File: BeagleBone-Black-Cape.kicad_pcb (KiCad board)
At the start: 4 copper layers, 61.9 x 92.1 mm, 77 parts, among them J501 Conn_ARM_JTAG_SWD_10, J502 3.3V, P101 BeagleBone_Black_Header, P102 BeagleBone_Black_Header, U401 LM3671, U601 cc1352p, U602 MX25R8035FZUIL0, Y601 32.768kHz, Y602 48MHz

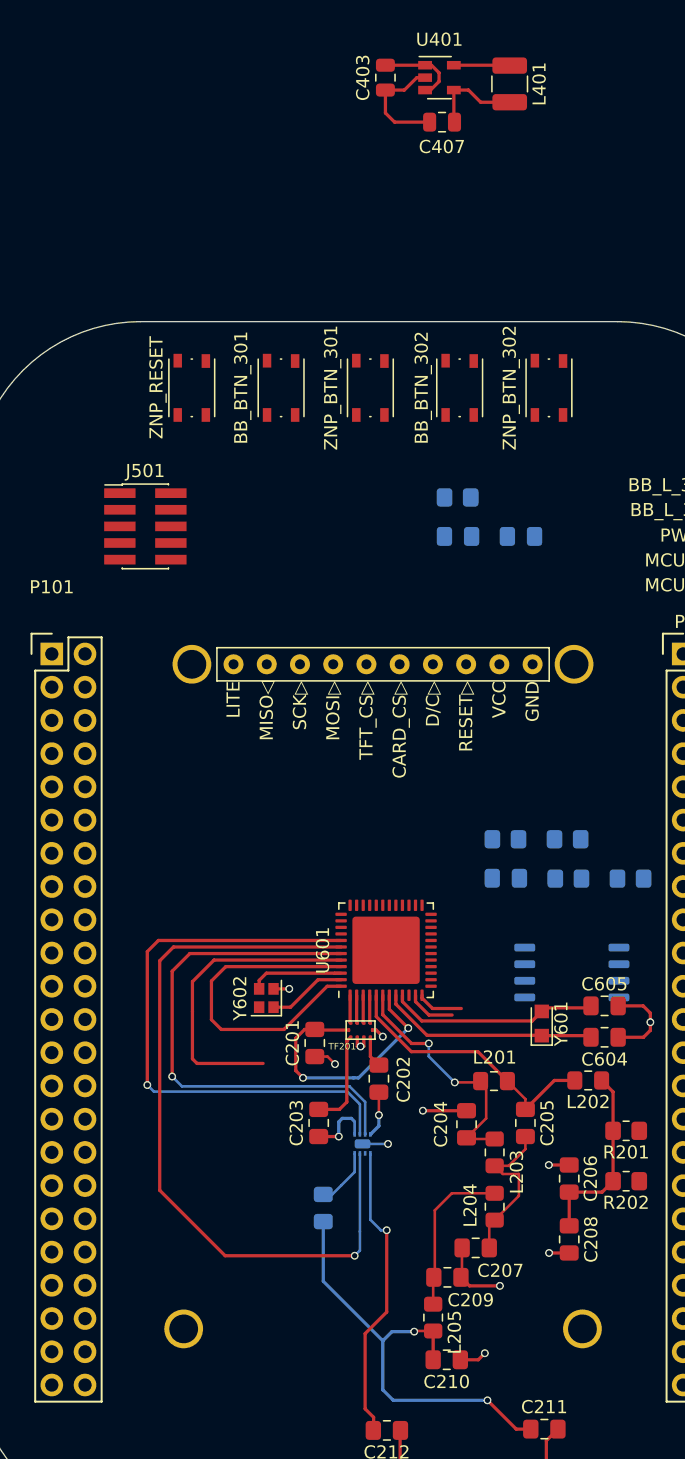
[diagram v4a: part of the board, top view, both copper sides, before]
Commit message: Connected PSUP, track lengths fixed for xtals
PSUP has been connected to power and ground planes. Traces have been made larger for that. The trace lengths have been matched for the xtals so that they should have the same properties.
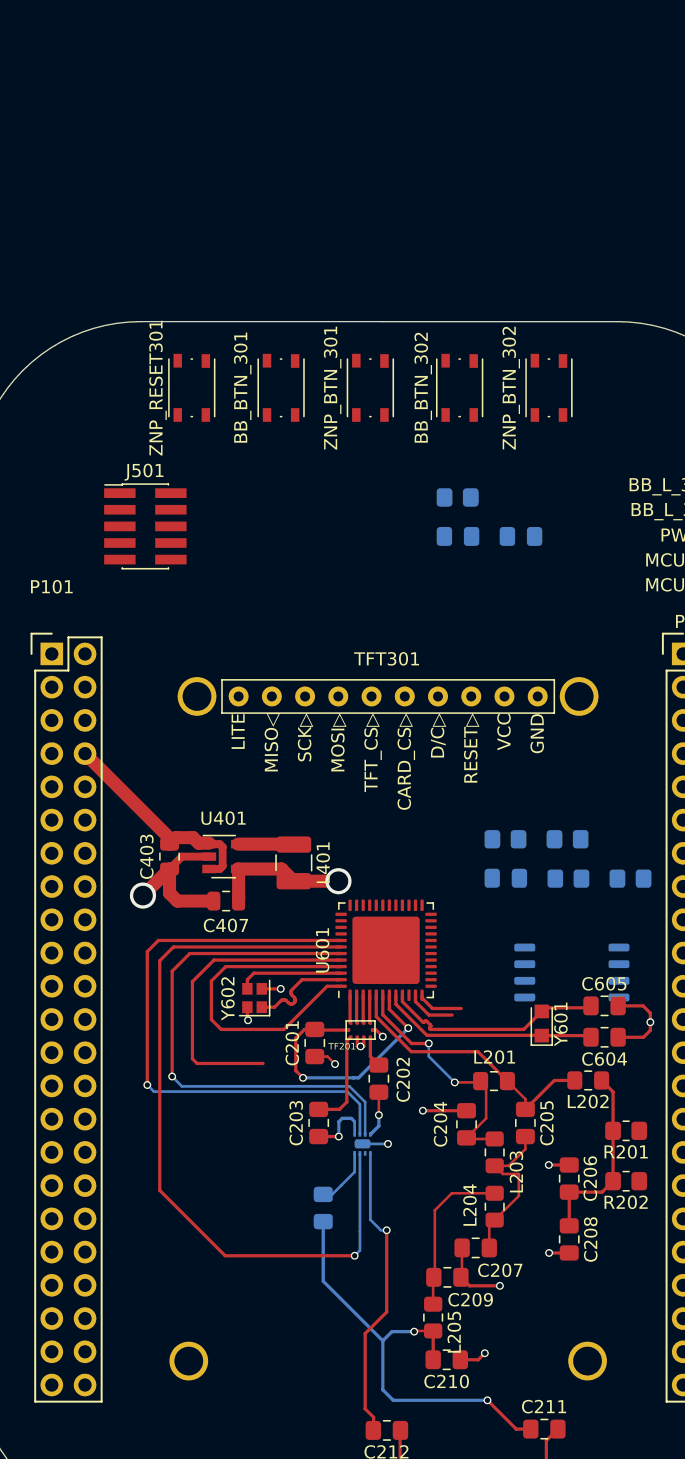
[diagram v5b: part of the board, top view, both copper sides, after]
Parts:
- moved C407 61.8 mm to (129.7, 81.3)
- moved L401 61.8 mm to (134.9, 78.4)
- moved C403 61.8 mm to (125.4, 77.9)
- moved U401 61.8 mm to (129.5, 77.9)
- moved TFT301 2.49 mm to (159.9, 63.1)
- moved Y602 0.90 mm to (131.9, 88.7)
- renumbered ZNP_RESET to ZNP_RESET301
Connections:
- J501 pad 7: (no net) -> Net-(J501-Pad7)
- P101 pad 10: (no net) -> SYS_RESETN
- P101 pad 17: (no net) -> Net-(P101-Pad17)
- P101 pad 18: (no net) -> Net-(P101-Pad18)
- P101 pad 19: (no net) -> Net-(P101-Pad19)
- P101 pad 20: (no net) -> Net-(P101-Pad20)
- P101 pad 21: (no net) -> Net-(P101-Pad21)
- P101 pad 22: (no net) -> Net-(P101-Pad22)
- P101 pad 23: (no net) -> Net-(P101-Pad23)
- P101 pad 25: (no net) -> Net-(P101-Pad25)
- P101 pad 27: (no net) -> Net-(P101-Pad27)
- P101 pad 32: (no net) -> Net-(P101-Pad32)
- P101 pad 33: (no net) -> Net-(P101-Pad33)
- P101 pad 34: (no net) -> Net-(P101-Pad34)
- P101 pad 35: (no net) -> Net-(P101-Pad35)
- P101 pad 36: (no net) -> Net-(P101-Pad36)
- P101 pad 37: (no net) -> Net-(P101-Pad37)
- P101 pad 38: (no net) -> Net-(P101-Pad38)
- P101 pad 39: (no net) -> Net-(P101-Pad39)
- P101 pad 40: (no net) -> Net-(P101-Pad40)
- P101 pad 41: (no net) -> Net-(P101-Pad41)
- P101 pad 42: (no net) -> Net-(P101-Pad42)
- P101 pad 9: (no net) -> PWR_BTN
- P102 pad 10: (no net) -> Net-(P102-Pad10)
- P102 pad 11: (no net) -> Net-(P102-Pad11)
- P102 pad 12: (no net) -> Net-(P102-Pad12)
- P102 pad 13: (no net) -> Net-(P102-Pad13)
- P102 pad 14: (no net) -> Net-(P102-Pad14)
- P102 pad 15: (no net) -> Net-(P102-Pad15)
- P102 pad 16: (no net) -> Net-(P102-Pad16)
- P102 pad 17: (no net) -> Net-(P102-Pad17)
- P102 pad 18: (no net) -> Net-(P102-Pad18)
- P102 pad 19: (no net) -> Net-(P102-Pad19)
- P102 pad 20: (no net) -> Net-(P102-Pad20)
- P102 pad 21: (no net) -> Net-(P102-Pad21)
- P102 pad 22: (no net) -> Net-(P102-Pad22)
- P102 pad 23: (no net) -> Net-(P102-Pad23)
- P102 pad 24: (no net) -> Net-(P102-Pad24)
- P102 pad 25: (no net) -> Net-(P102-Pad25)
- P102 pad 26: (no net) -> Net-(P102-Pad26)
- P102 pad 27: (no net) -> Net-(P102-Pad27)
- P102 pad 28: (no net) -> Net-(P102-Pad28)
- P102 pad 29: (no net) -> Net-(P102-Pad29)
- P102 pad 3: (no net) -> Net-(P102-Pad3)
- P102 pad 30: (no net) -> Net-(P102-Pad30)
- P102 pad 31: (no net) -> Net-(P102-Pad31)
- P102 pad 32: (no net) -> Net-(P102-Pad32)
- P102 pad 33: (no net) -> Net-(P102-Pad33)
- P102 pad 34: (no net) -> Net-(P102-Pad34)
- P102 pad 35: (no net) -> Net-(P102-Pad35)
- P102 pad 36: (no net) -> Net-(P102-Pad36)
- P102 pad 37: (no net) -> Net-(P102-Pad37)
- P102 pad 38: (no net) -> Net-(P102-Pad38)
- P102 pad 39: (no net) -> Net-(P102-Pad39)
- P102 pad 4: (no net) -> Net-(P102-Pad4)
- P102 pad 40: (no net) -> Net-(P102-Pad40)
- P102 pad 41: (no net) -> Net-(P102-Pad41)
- P102 pad 42: (no net) -> Net-(P102-Pad42)
- P102 pad 43: (no net) -> Net-(P102-Pad43)
- P102 pad 44: (no net) -> Net-(P102-Pad44)
- P102 pad 45: (no net) -> Net-(P102-Pad45)
- P102 pad 46: (no net) -> Net-(P102-Pad46)
- P102 pad 5: (no net) -> Net-(P102-Pad5)
- P102 pad 6: (no net) -> Net-(P102-Pad6)
- P102 pad 7: (no net) -> Net-(P102-Pad7)
- P102 pad 8: (no net) -> Net-(P102-Pad8)
- P102 pad 9: (no net) -> Net-(P102-Pad9)
- R201 pad 1: (no net) -> Net-(R201-Pad1)
- R202 pad 1: (no net) -> Net-(R202-Pad1)
- TF202 pad 2: (no net) -> Net-(TF202-Pad2)
- TFT301 pad 6: (no net) -> Net-(TFT301-Pad6)
- U601 pad 10: (no net) -> Net-(U601-Pad10)
- U601 pad 17: (no net) -> Net-(U601-Pad17)
- U601 pad 28: (no net) -> Net-(U601-Pad28)
- U601 pad 29: (no net) -> Net-(U601-Pad29)
- U601 pad 31: (no net) -> Net-(U601-Pad31)
- U601 pad 32: (no net) -> Net-(U601-Pad32)
- U601 pad 36: (no net) -> Net-(U601-Pad36)
- U601 pad 37: (no net) -> Net-(U601-Pad37)
- U601 pad 38: (no net) -> Net-(U601-Pad38)
- U601 pad 39: (no net) -> Net-(U601-Pad39)
- U601 pad 40: (no net) -> Net-(U601-Pad40)
- U601 pad 6: (no net) -> RX_20dB_N
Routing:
- net SYS_5V: track 6.35 -> 16.7 mm
- net MCU_VDD: track 7.13 -> 10.5 mm, vias 0 -> 1
- net GND: track 66.9 -> 69.9 mm, vias 11 -> 12
- net X48M_P: track 6.03 -> 8.07 mm
- net (no net): track 10.2 -> 11.2 mm, vias 2 -> 3
- net X48M_N: track 7.14 -> 8.07 mm
- net X32K_Q2: track 16.0 -> 16.8 mm

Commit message: MOST CURRENT. NEED TO PLACE MORE STUFF
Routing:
- net Net-(U601-Pad38): track 0.00 -> 5.92 mm, vias 0 -> 1
- net Net-(U601-Pad39): track 0.00 -> 5.87 mm, vias 0 -> 1
- net Net-(U601-Pad40): track 0.00 -> 5.82 mm, vias 0 -> 1
- net Net-(U601-Pad37): track 0.00 -> 5.76 mm, vias 0 -> 1
- net Net-(U601-Pad36): track 0.00 -> 4.31 mm, vias 0 -> 1
- net Net-(U601-Pad32): track 0.00 -> 4.31 mm, vias 0 -> 1
- net VDDR: track 24.9 -> 25.9 mm
- net MCU_VDD: track 10.5 -> 9.96 mm

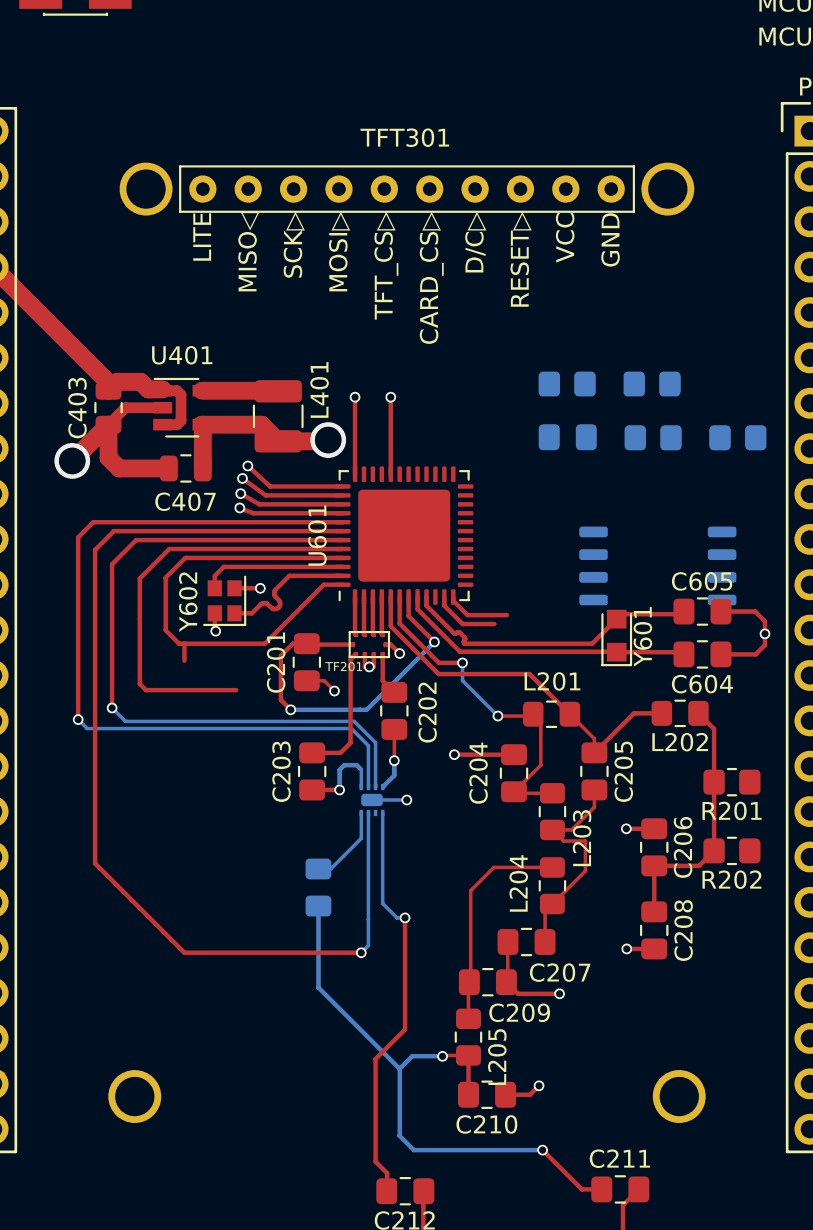
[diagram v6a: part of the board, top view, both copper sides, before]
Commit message: Centered TFT display on the board
Centered the TFT display on the board. The footprint was modified so the origin was the center of the component.
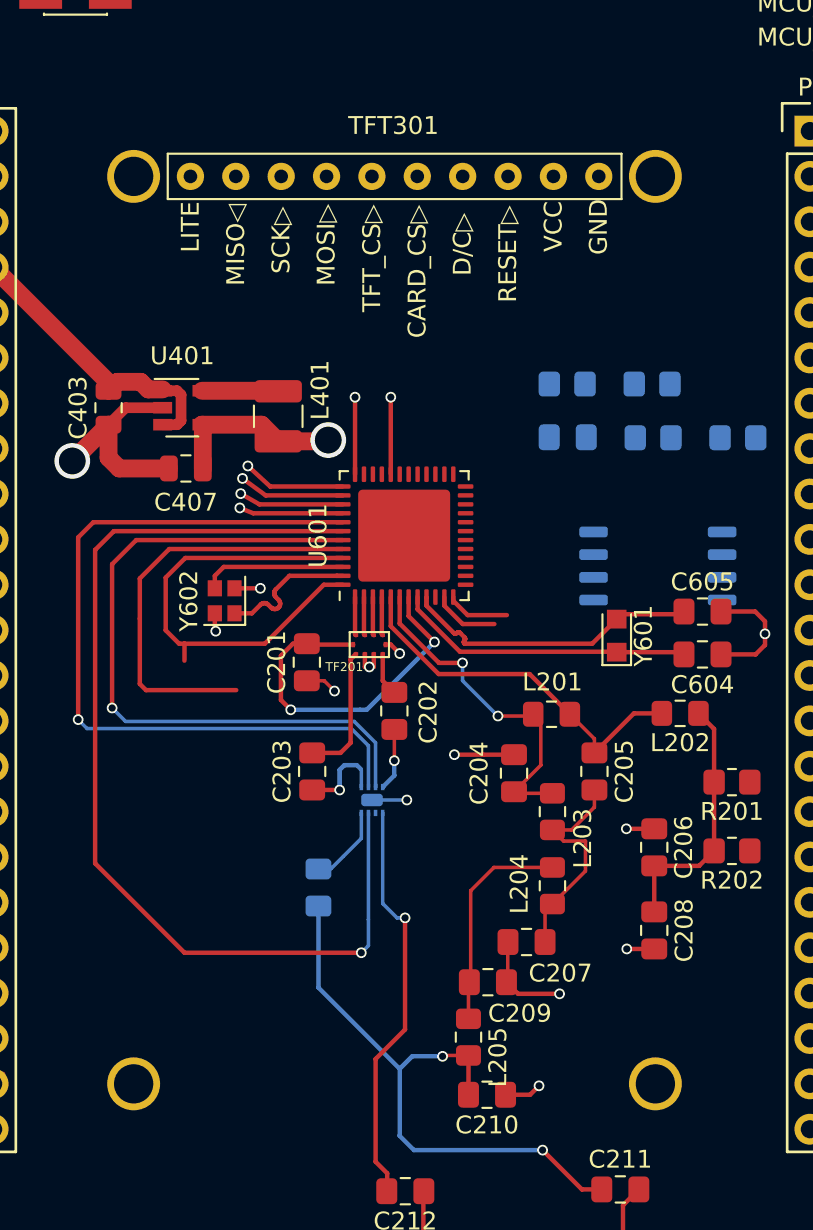
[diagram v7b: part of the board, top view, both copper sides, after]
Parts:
- moved TFT301 32.9 mm to (141.4, 90.3)

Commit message: Added more connections and other changes
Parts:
- removed BB_L_301, MCU_L_301: LED, LED_SMD:LED_0603_1608Metric_Pad1.05x0.95mm_HandSolder
- added BB_USER2: LED, LED_SMD:LED_0603_1608Metric_Pad1.05x0.95mm_HandSolder, F.Cu at (167.2, 57.0)
- added RX: LED, LED_SMD:LED_0603_1608Metric_Pad1.05x0.95mm_HandSolder, F.Cu at (167.3, 51.8)
- FB401: moved to F.Cu
- moved FB401 76.6 mm to (127.1, 89.5), turned to 270 degrees
- moved BB_USER1 6.07 mm to (167.3, 55.3)
- moved TX 4.01 mm to (167.3, 53.6)
- moved PWR 3.63 mm to (167.4, 50.1)
- renumbered BB_BTN_302 to BB_BTN, BB_BTN_301 to BB_BTN, BB_L_302 to BB_USER1, PWR301 to PWR, MCU_L_302 to TX, ZNP_BTN_302 to ZNP_BTN, ZNP_BTN_301 to ZNP_BTN, ZNP_RESET301 to ZNP_RESET
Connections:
- Y602 pad 4: (no net) -> GND
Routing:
- net SCK_TFT: track 0.00 -> 65.3 mm
- net MISO_TFT: track 0.00 -> 58.7 mm
- net D.C_TFT: track 0.00 -> 45.0 mm
- net MOSI_TFT: track 0.00 -> 42.4 mm
- net CS_TFT: track 0.00 -> 39.3 mm
- net RST_TFT: track 0.00 -> 38.0 mm
- net VDDS: track 23.5 -> 13.2 mm
- net MCU_VDD: track 9.96 -> 17.9 mm, vias 1 -> 4
- net GND: track 69.9 -> 73.5 mm, vias 12 -> 14
- net SKY_V3_2G4: track 44.5 -> 42.3 mm
- net SKY_V1_20DBM: track 56.8 -> 55.2 mm
- net (no net): track 11.2 -> 10.2 mm, vias 3 -> 2
- net SKY_V2_SUB1G: track 39.6 -> 38.6 mm
